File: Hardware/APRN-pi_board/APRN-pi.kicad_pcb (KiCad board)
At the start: 2 copper layers, 65 x 56.5 mm, 21 parts, among them J1 Raspberry_Pi_2_3, J2 Conn_Coaxial, J3 Amplifier Jumper, Q1 2N3906, U1 DRA818V

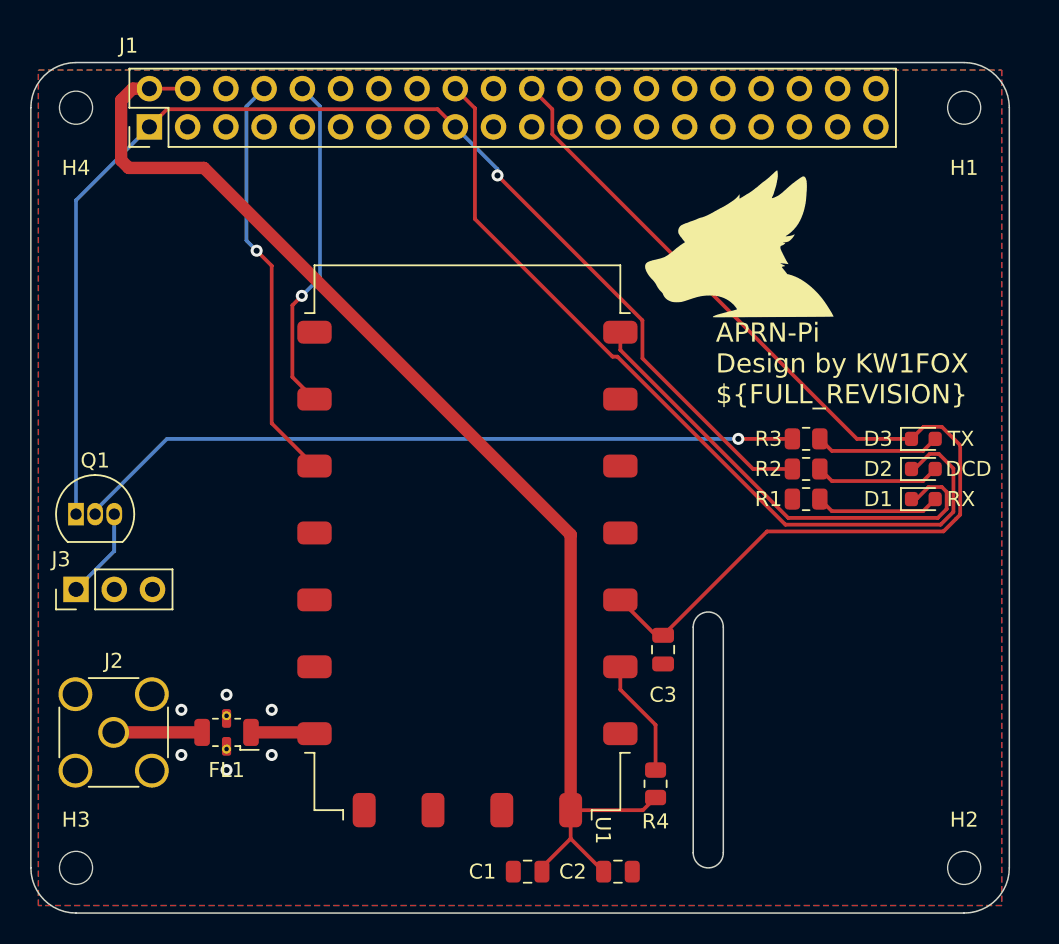
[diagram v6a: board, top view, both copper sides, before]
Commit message: Flip header correct direction
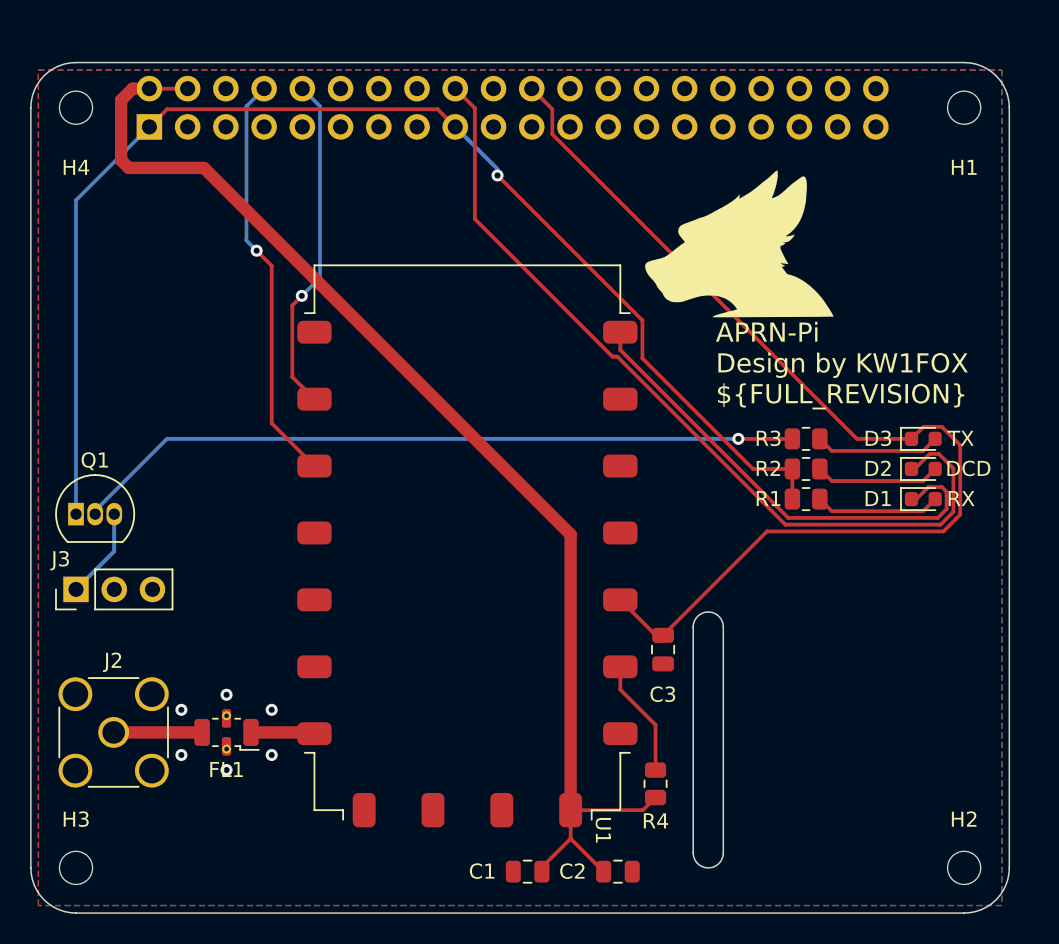
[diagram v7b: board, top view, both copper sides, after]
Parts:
- J1: footprint Connector_PinHeader_2.54mm:PinHeader_2x20_P2.54mm_Vertical -> Connector_PinSocket_2.54mm:PinSocket_2x20_P2.54mm_Vertical; moved to B.Cu
- turned J1 to -90 degrees
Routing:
- net +3V3: track 82.6 -> 84.6 mm

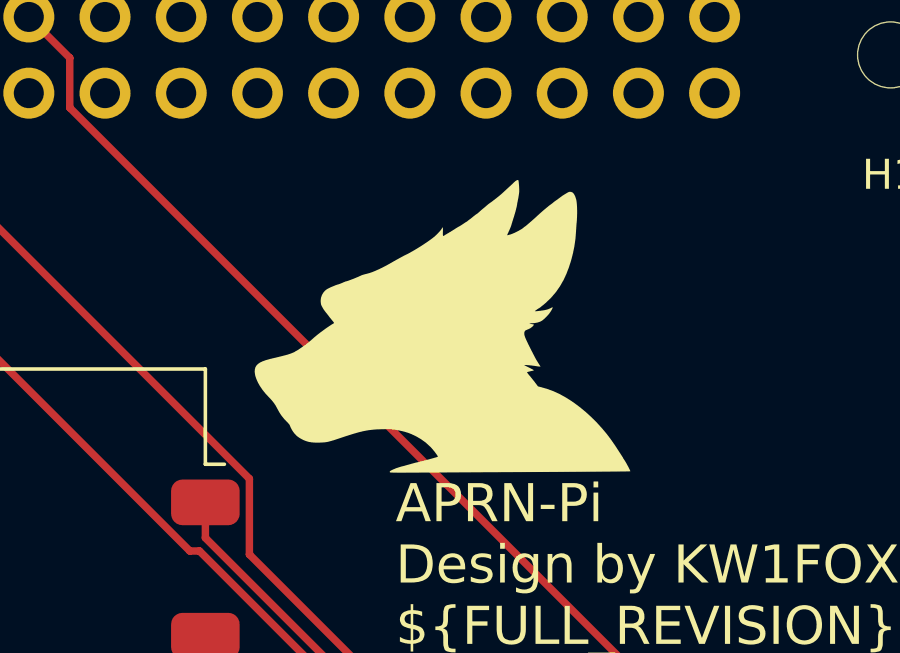
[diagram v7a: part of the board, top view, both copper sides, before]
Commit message: Scootch logo
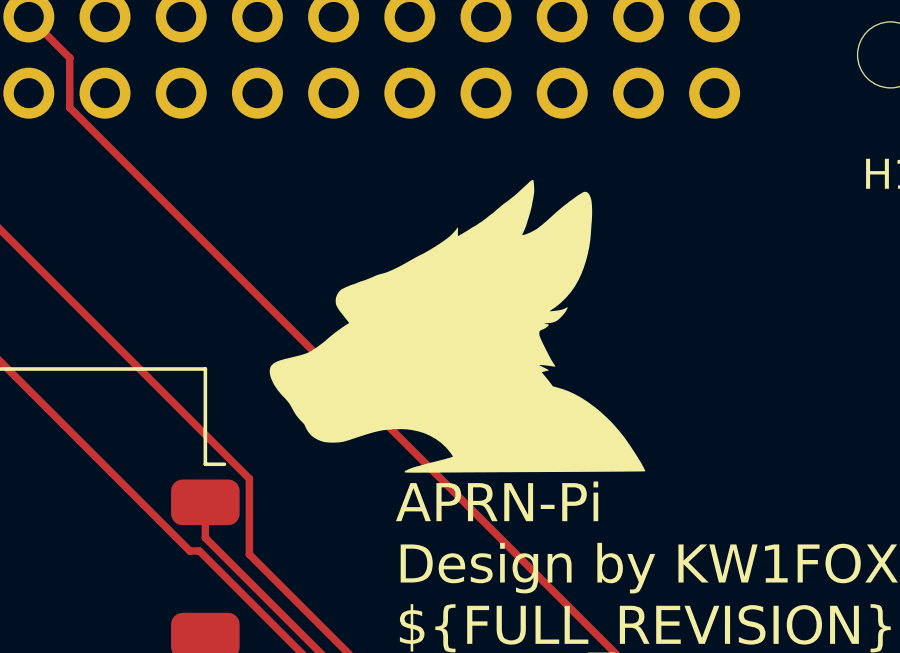
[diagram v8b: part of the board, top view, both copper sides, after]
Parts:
- moved L1 0.50 mm to (156.5, 77.0)
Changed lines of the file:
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@@
   )
   (footprint "KenwoodFox:KITSUNE_LOGO" (layer "F.Cu")
-    (at 156 77)
+    (at 156.5 77)
     (property "Sheetfile" "APRN-pi.kicad_sch")
     (property "Sheetname" "")
